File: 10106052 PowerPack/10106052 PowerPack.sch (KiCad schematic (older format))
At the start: 0 parts

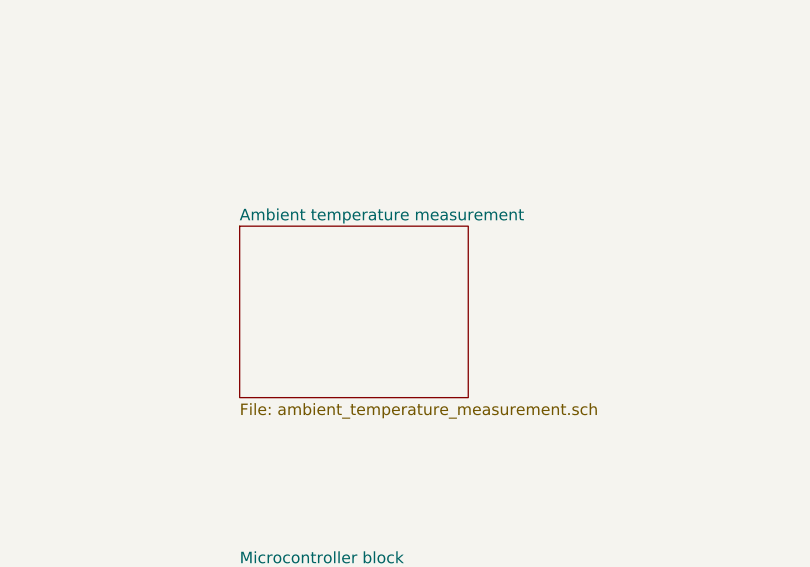
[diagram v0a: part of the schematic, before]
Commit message: temperature measurement schematic added
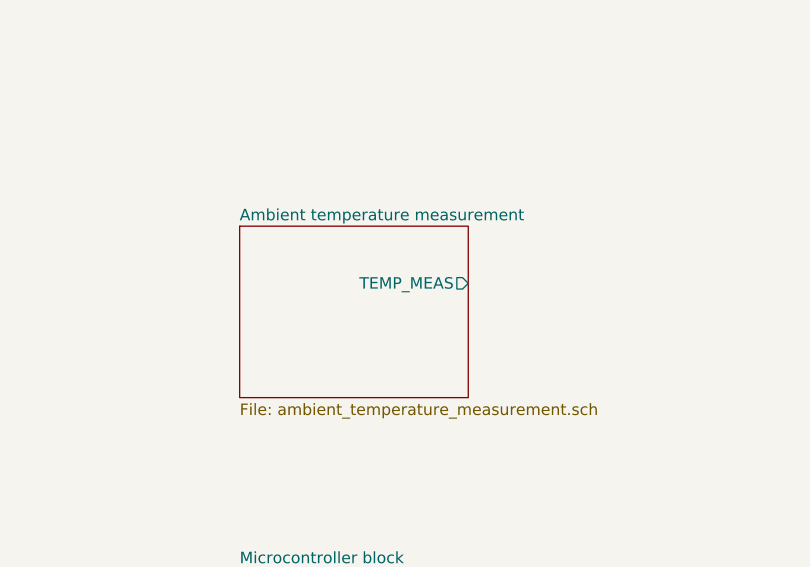
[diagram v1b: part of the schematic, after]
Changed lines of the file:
@@
 F0 "Ambient temperature measurement" 50
 F1 "ambient_temperature_measurement.sch" 50
+F2 "TEMP_MEAS" O R 6250 2500 50
 $EndSheet
 $EndSCHEMATC

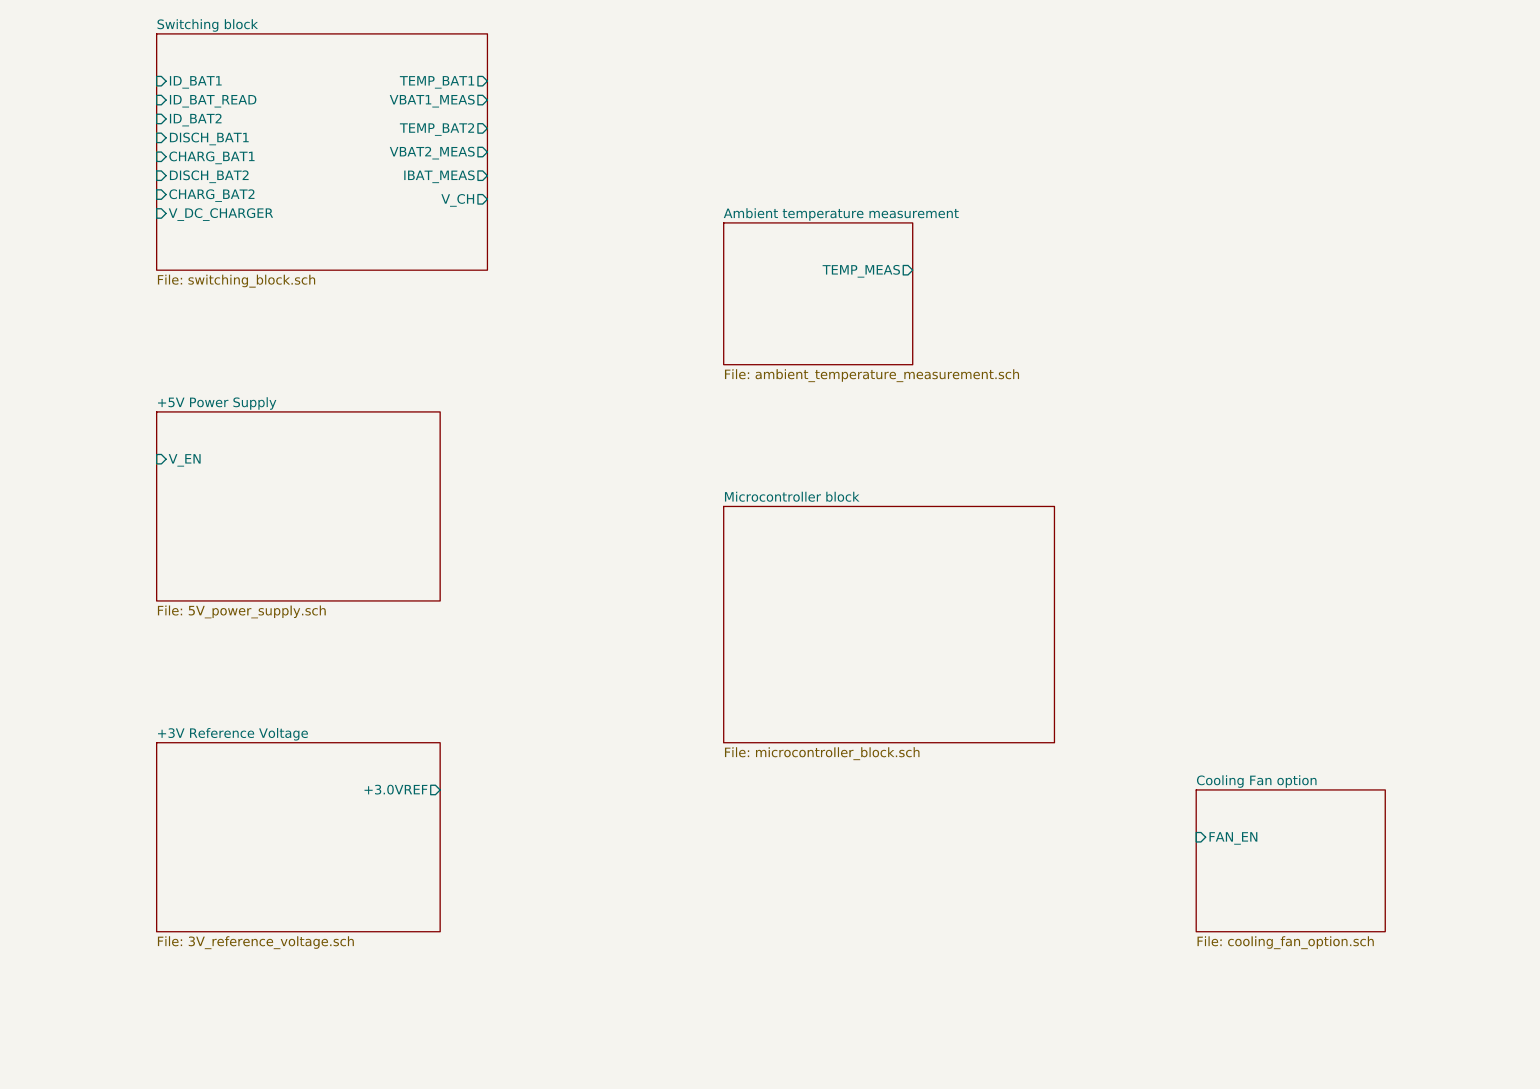
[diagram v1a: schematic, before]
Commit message: PowerPack schematic toplevel done
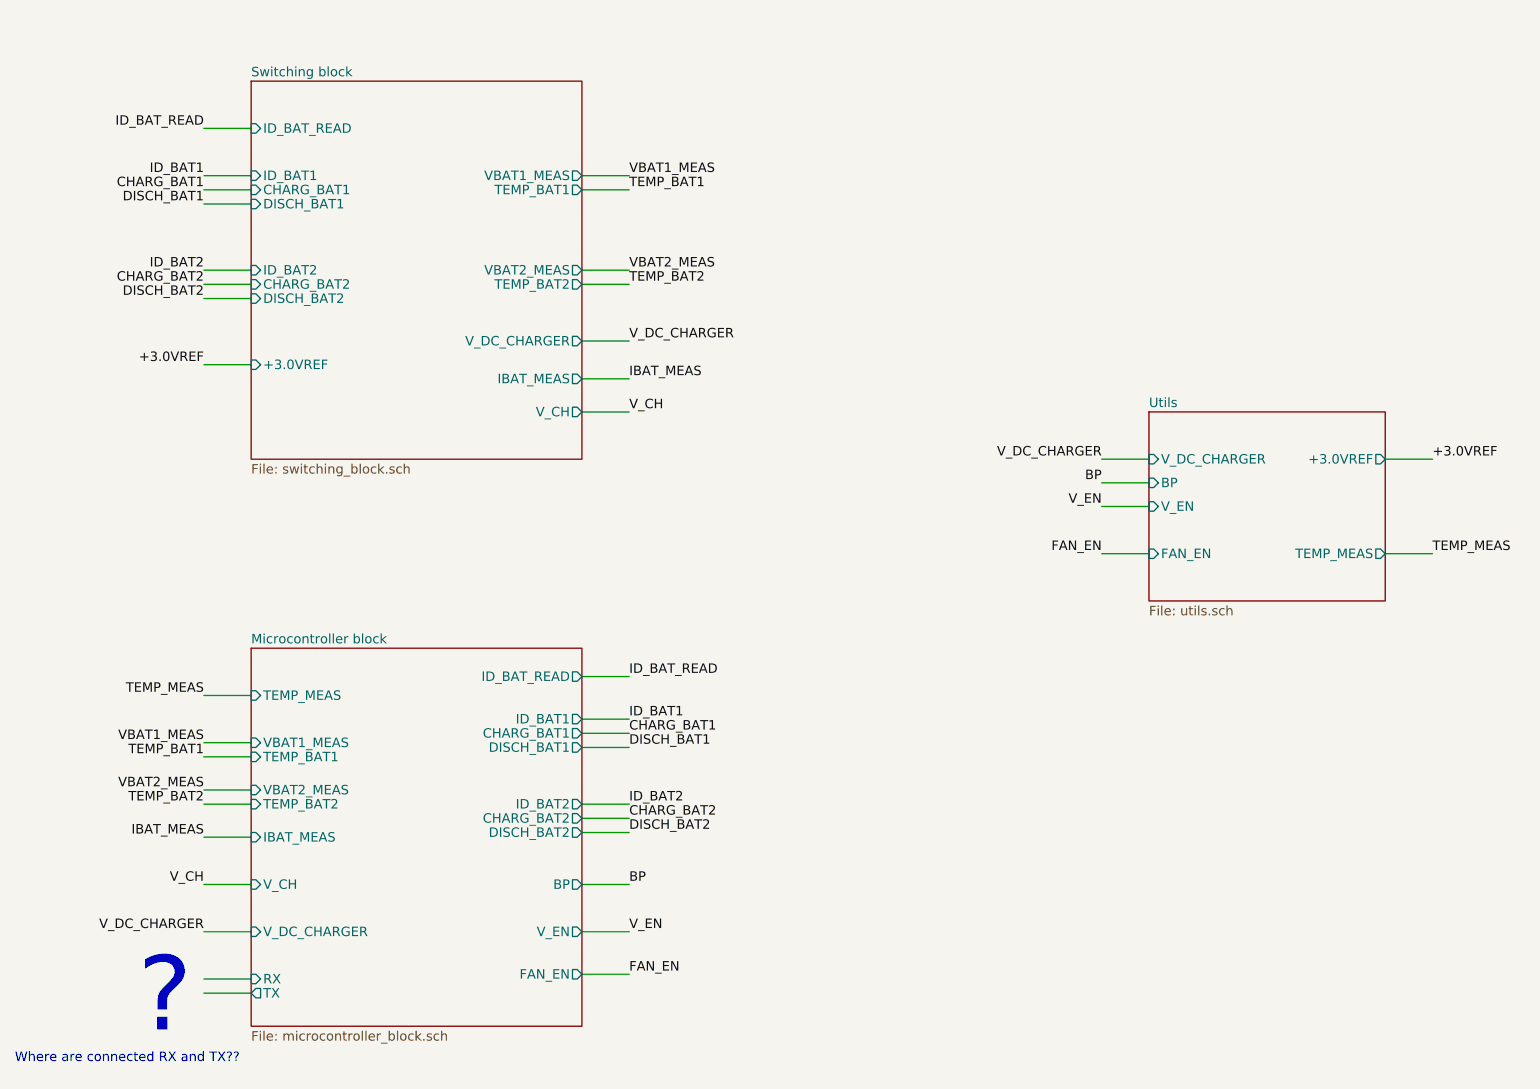
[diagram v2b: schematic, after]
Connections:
- net labels added: +3.0VREF, BP, CHARG_BAT1, CHARG_BAT2, DISCH_BAT1, DISCH_BAT2, FAN_EN, IBAT_MEAS, ID_BAT1, ID_BAT2, ID_BAT_READ, TEMP_BAT1, TEMP_BAT2, TEMP_MEAS, VBAT1_MEAS, VBAT2_MEAS, V_CH, V_DC_CHARGER, V_EN
- wire segments 0 -> 41
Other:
- note added: "?"
- note added: "Where are connected RX and TX??"

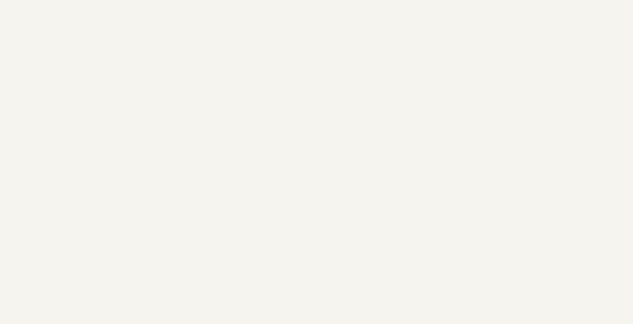
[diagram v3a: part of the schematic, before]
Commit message: Import drawing as Cmts.User layer
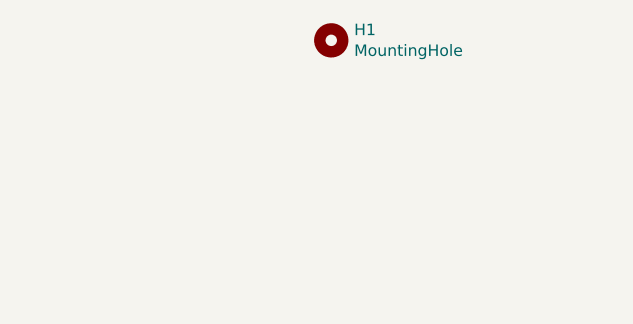
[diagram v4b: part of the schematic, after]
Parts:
- added H1: MountingHole, MountingHole:MountingHole_3.2mm_M3_ISO7380, symbol Mechanical:MountingHole
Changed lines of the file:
@@
 Text Notes 1500 6700 0    50   ~ 0
 Where are connected RX and TX??
+$Comp
+L Mechanical:MountingHole H1
+U 1 1 5E8A1129
+P 8250 1250
+F 0 "H1" H 8350 1296 50  0000 L CNN
+F 1 "MountingHole" H 8350 1205 50  0000 L CNN
+F 2 "MountingHole:MountingHole_3.2mm_M3_ISO7380" H 8250 1250 50  0001 C CNN
+F 3 "~" H 8250 1250 50  0001 C CNN
+	1    8250 1250
+	1    0    0    -1
+$EndComp
 $EndSCHEMATC

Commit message: Footprints relinked
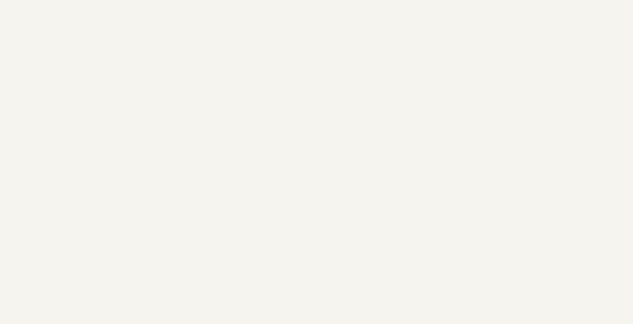
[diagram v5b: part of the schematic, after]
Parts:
- removed H1: MountingHole, MountingHole:MountingHole_3.2mm_M3_ISO7380, symbol Mechanical:MountingHole
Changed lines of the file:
@@
 Text Notes 1500 6700 0    50   ~ 0
 Where are connected RX and TX??
-$Comp
-L Mechanical:MountingHole H1
-U 1 1 5E8A1129
-P 8250 1250
-F 0 "H1" H 8350 1296 50  0000 L CNN
-F 1 "MountingHole" H 8350 1205 50  0000 L CNN
-F 2 "MountingHole:MountingHole_3.2mm_M3_ISO7380" H 8250 1250 50  0001 C CNN
-F 3 "~" H 8250 1250 50  0001 C CNN
-	1    8250 1250
-	1    0    0    -1
-$EndComp
 $EndSCHEMATC

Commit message: powerpack-dev
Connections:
- wire segments 41 -> 39
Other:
- note removed: "?"
- note removed: "Where are connected RX and TX??"
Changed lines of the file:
@@
 F8 "TEMP_MEAS" I L 2750 4750 50
 F9 "V_CH" I L 2750 5750 50
-F10 "RX" I L 2750 6250 50
-F11 "TX" O L 2750 6325 50
-F12 "V_EN" O R 4500 6000 50
-F13 "TEMP_BAT2" I L 2750 5325 50
-F14 "TEMP_BAT1" I L 2750 5075 50
-F15 "FAN_EN" O R 4500 6225 50
-F16 "ID_BAT1" O R 4500 4875 50
-F17 "ID_BAT2" O R 4500 5325 50
-F18 "VBAT1_MEAS" I L 2750 5000 50
-F19 "VBAT2_MEAS" I L 2750 5250 50
-F20 "IBAT_MEAS" I L 2750 5500 50
-F21 "DISCH_BAT2" O R 4500 5475 50
+F10 "V_EN" O R 4500 6000 50
+F11 "TEMP_BAT2" I L 2750 5325 50
+F12 "TEMP_BAT1" I L 2750 5075 50
+F13 "FAN_EN" O R 4500 6225 50
+F14 "ID_BAT1" O R 4500 4875 50
+F15 "ID_BAT2" O R 4500 5325 50
+F16 "VBAT1_MEAS" I L 2750 5000 50
+F17 "VBAT2_MEAS" I L 2750 5250 50
+F18 "IBAT_MEAS" I L 2750 5500 50
+F19 "DISCH_BAT2" O R 4500 5475 50
 $EndSheet
 Wire Wire Line
@@
 Wire Wire Line
 	2750 6000 2500 6000
-Wire Wire Line
-	2750 6250 2500 6250
-Wire Wire Line
-	2750 6325 2500 6325
 Wire Wire Line
 	4750 6225 4500 6225
@@
 Text Label 2500 5750 2    50   ~ 0
 V_CH
-Text Notes 2150 6575 0    394  ~ 0
-?
 Text Label 7250 3625 2    50   ~ 0
 BP
@@
 Text Label 4750 6225 0    50   ~ 0
 FAN_EN
-Text Notes 1500 6700 0    50   ~ 0
-Where are connected RX and TX??
 $EndSCHEMATC

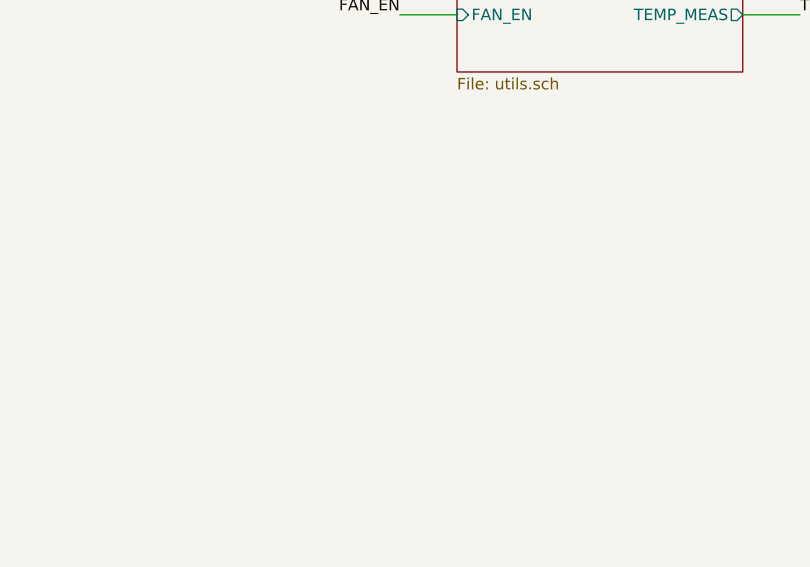
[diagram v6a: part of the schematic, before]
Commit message: add fiducials and mt holes to schematic
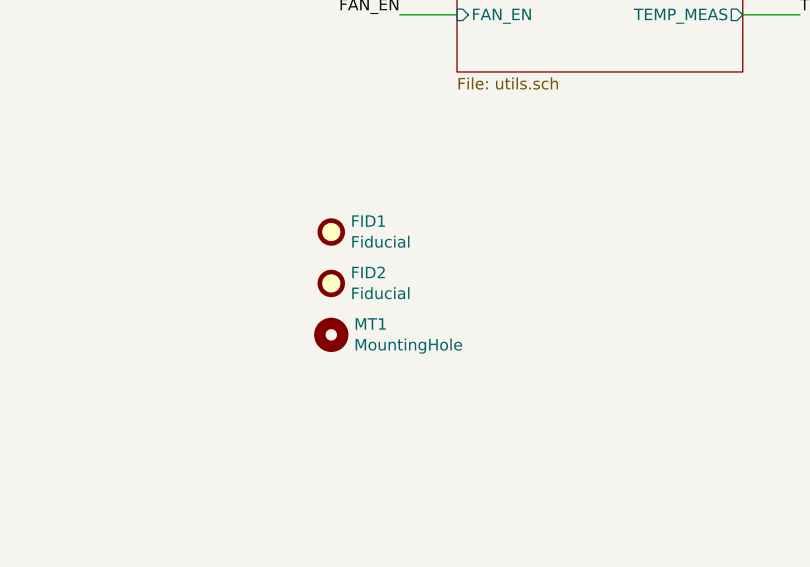
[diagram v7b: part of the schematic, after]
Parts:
- added FID1, FID2: Fiducial, AllModules:FIDUCIAL, symbol Mechanical:Fiducial
- added MT1: MountingHole, AllModules:MTHOLE1, symbol Mechanical:MountingHole
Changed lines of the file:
@@
 Text Label 4750 6225 0    50   ~ 0
 FAN_EN
+$Comp
+L Mechanical:Fiducial FID1
+U 1 1 5EA07F53
+P 6950 4950
+F 0 "FID1" H 7035 4996 50  0000 L CNN
+F 1 "Fiducial" H 7035 4905 50  0000 L CNN
+F 2 "AllModules:FIDUCIAL" H 6950 4950 50  0001 C CNN
+F 3 "~" H 6950 4950 50  0001 C CNN
+	1    6950 4950
+	1    0    0    -1
+$EndComp
+$Comp
+L Mechanical:Fiducial FID2
+U 1 1 5EA08287
+P 6950 5175
+F 0 "FID2" H 7035 5221 50  0000 L CNN
+F 1 "Fiducial" H 7035 5130 50  0000 L CNN
+F 2 "AllModules:FIDUCIAL" H 6950 5175 50  0001 C CNN
+F 3 "~" H 6950 5175 50  0001 C CNN
+	1    6950 5175
+	1    0    0    -1
+$EndComp
+$Comp
+L Mechanical:MountingHole MT1
+U 1 1 5EA08596
+P 6950 5400
+F 0 "MT1" H 7050 5446 50  0000 L CNN
+F 1 "MountingHole" H 7050 5355 50  0000 L CNN
+F 2 "AllModules:MTHOLE1" H 6950 5400 50  0001 C CNN
+F 3 "~" H 6950 5400 50  0001 C CNN
+	1    6950 5400
+	1    0    0    -1
+$EndComp
 $EndSCHEMATC

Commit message: sync values
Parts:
- FID1, FID2: value Fiducial -> FIDUCIAL
- MT1: value MountingHole -> MTHOLE1
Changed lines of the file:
@@
 P 6950 4950
 F 0 "FID1" H 7035 4996 50  0000 L CNN
-F 1 "Fiducial" H 7035 4905 50  0000 L CNN
+F 1 "FIDUCIAL" H 7035 4905 50  0000 L CNN
 F 2 "AllModules:FIDUCIAL" H 6950 4950 50  0001 C CNN
 F 3 "~" H 6950 4950 50  0001 C CNN
@@
 P 6950 5175
 F 0 "FID2" H 7035 5221 50  0000 L CNN
-F 1 "Fiducial" H 7035 5130 50  0000 L CNN
+F 1 "FIDUCIAL" H 7035 5130 50  0000 L CNN
 F 2 "AllModules:FIDUCIAL" H 6950 5175 50  0001 C CNN
 F 3 "~" H 6950 5175 50  0001 C CNN
@@
 P 6950 5400
 F 0 "MT1" H 7050 5446 50  0000 L CNN
-F 1 "MountingHole" H 7050 5355 50  0000 L CNN
+F 1 "MTHOLE1" H 7050 5355 50  0000 L CNN
 F 2 "AllModules:MTHOLE1" H 6950 5400 50  0001 C CNN
 F 3 "~" H 6950 5400 50  0001 C CNN
